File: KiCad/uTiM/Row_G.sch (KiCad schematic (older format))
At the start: 10 parts, among them U701 APA102, U702 APA102, U703 APA102, U704 APA102, U705 APA102, U706 APA102, U707 APA102, U708 APA102

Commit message: microTiM aka uTiM work in progress
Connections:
- net CO_G renamed CI_H
- net DO_G renamed DI_H
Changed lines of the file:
@@
 DI_G
 Text HLabel 950  3100 0    60   Output ~ 12
-CO_G
+CI_H
 Text HLabel 950  2350 0    60   Input ~ 12
 GND
@@
 5V
 Text Label 1075 3100 0    60   ~ 0
-CO_G
+CI_H
 $Comp
 L GND #PWR05
@@
 	10950 3350 950  3350
 Text HLabel 950  3350 0    60   Output ~ 12
-DO_G
+DI_H
 Text HLabel 950  1400 0    60   Input ~ 12
 DI_G
@@
 	1300 1600 950  1600
 Text Label 1075 3350 0    60   ~ 0
-DO_G
+DI_H
 Text Label 1075 1600 0    60   ~ 0
 CI_G

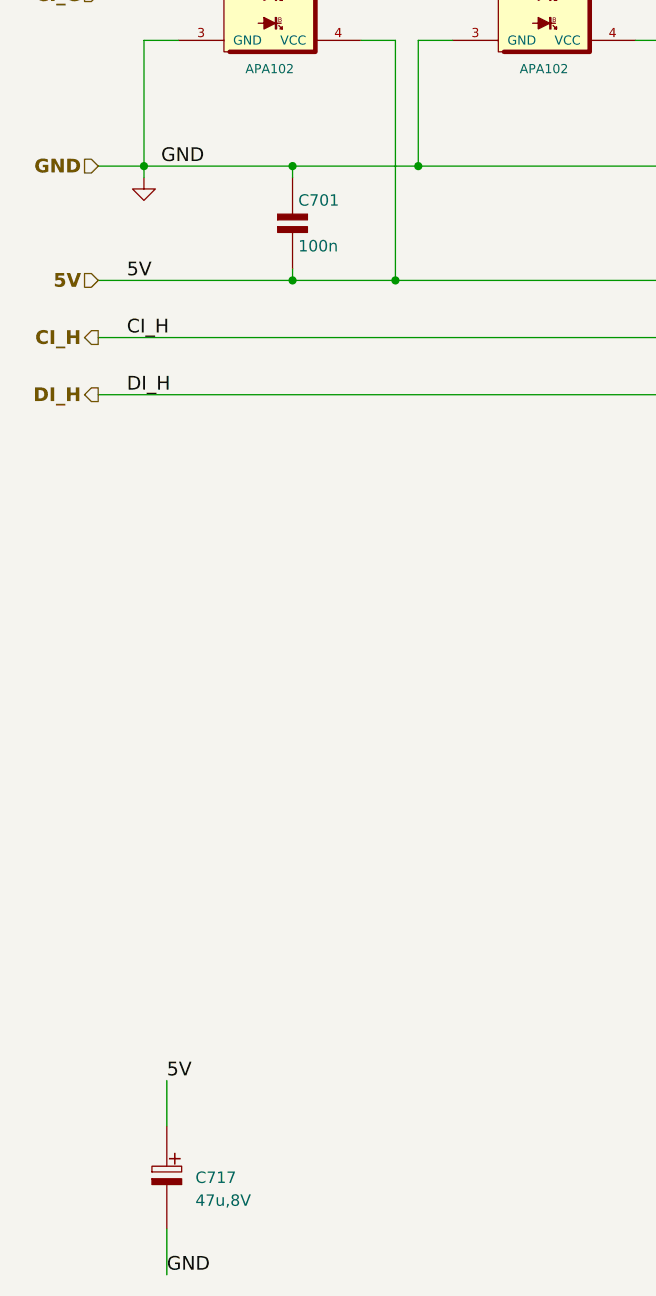
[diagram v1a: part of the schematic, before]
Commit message: work in progress, microTIM using APA102
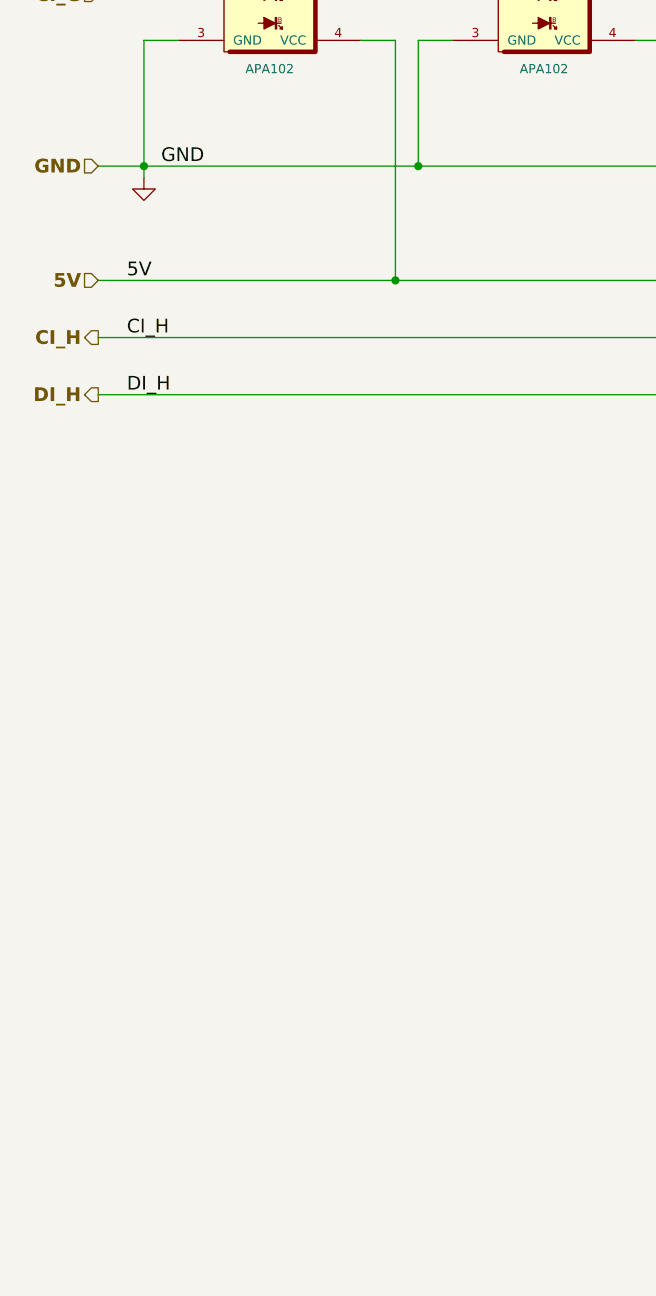
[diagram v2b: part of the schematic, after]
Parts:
- removed C701: 100n, TinyTiM_Libs:c_0805, symbol C2
- removed C717: 47u,8V, TinyTiM_Libs:c_2917, symbol C_POL_1
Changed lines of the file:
@@
 Comment4 ""
 $EndDescr
-$Comp
-L C2 C701
-U 1 1 5118AB56
-P 1800 2600
-F 0 "C701" H 1825 2700 50  0000 L CNN
-F 1 "100n" H 1825 2500 50  0000 L CNN
-F 2 "TinyTiM_Libs:c_0805" H 1800 2600 50  0001 C CNN
-F 3 "" H 1800 2600 60  0001 C CNN
-F 4 "CAP CER 0.1UF 25V 10% X7R 0805" H 1800 2800 60  0001 L CNN "Field4"
-F 5 "100nF, 25V" H 1800 2900 60  0001 L CNN "Field5"
-F 6 "Surface Mount, MLCC" H 1800 3000 60  0001 L CNN "Field6"
-F 7 "Kemet" H 1800 3100 60  0001 L CNN "Field7"
-F 8 "C0805C104K3RACTU" H 1800 3200 60  0001 L CNN "Field8"
-F 9 "Digikey" H 1800 3300 60  0001 L CNN "Field9"
-F 10 "399-1168-1-ND" H 1800 3400 60  0001 L CNN "Field10"
-F 11 "http://www.digikey.com/product-detail/en/C0805C104K3RACTU/399-1168-1-ND/411443" H 1800 3500 60  0001 L CNN "Field11"
-	1    1800 2600
-	1    0    0    -1
-$EndComp
-Text Label 1250 6350 0    60   ~ 0
-5V
-Text Label 1250 7200 0    60   ~ 0
-GND
-$Comp
-L C_POL_1 C717
-U 1 1 5118AB60
-P 1250 6750
-F 0 "C717" H 1375 6725 50  0000 L CNN
-F 1 "47u,8V" H 1375 6625 50  0000 L CNN
-F 2 "TinyTiM_Libs:c_2917" H 1250 6700 50  0001 C CNN
-F 3 "" H 1250 6750 60  0001 C CNN
-F 4 "CAP ALUM 47UF 8V 20% SMD" H 1250 6950 60  0001 L CNN "Field4"
-F 5 "47u,8V" H 1250 7050 60  0001 L CNN "Field5"
-F 6 "2917 (7343 Metric)" H 1250 7150 60  0001 L CNN "Field6"
-F 7 "Panasonic Electronic Components" H 1250 7250 60  0001 L CNN "Field7"
-F 8 "EEF-CD0K470R" H 1250 7350 60  0001 L CNN "Field8"
-F 9 "Digikey" H 1250 7450 60  0001 L CNN "Field9"
-F 10 "PCE3606CT-ND" H 1250 7550 60  0001 L CNN "Field10"
-F 11 "http://www.digikey.com/product-detail/en/EEF-CD0K470R/PCE3606CT-ND/614442" H 1250 7650 60  0001 L CNN "Field11"
-	1    1250 6750
-	1    0    0    -1
-$EndComp
-Wire Wire Line
-	1250 7000 1250 7200
-Wire Wire Line
-	1250 6550 1250 6350
 Text Label 1075 1400 0    60   ~ 0
 DI_G
@@
 Wire Wire Line
 	1150 1800 1150 2400
-Connection ~ 1800 2850
-Wire Wire Line
-	1800 2850 1800 2800
 Wire Wire Line
 	950  3100 10800 3100
-Connection ~ 1800 2350
 Wire Wire Line
 	950  2350 9550 2350
@@
 	10800 3100 10800 1600
 Wire Wire Line
-	1800 2350 1800 2400
-Wire Wire Line
 	950  2850 10650 2850

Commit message: layout complete. Gerbers pending
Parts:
- renumbered U701 to U49, U702 to U50, U703 to U51, U704 to U52, U705 to U53, U706 to U54, U707 to U55, U708 to U56
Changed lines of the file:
@@
 GND
 $Comp
-L APA102 U701
+L APA102 U49
 U 1 1 56C1D372
 P 1700 1600
-F 0 "U701" H 1700 1900 40  0000 C CNB
+F 0 "U49" H 1700 1900 40  0000 C CNB
 F 1 "APA102" H 1700 1275 40  0000 C CNN
 F 2 "TinyTiM_Libs:APA102" H 1600 2000 60  0001 C CNN
@@
 5V
 $Comp
-L APA102 U702
+L APA102 U50
 U 1 1 56C1D39D
 P 2900 1600
-F 0 "U702" H 2900 1900 40  0000 C CNB
+F 0 "U50" H 2900 1900 40  0000 C CNB
 F 1 "APA102" H 2900 1275 40  0000 C CNN
 F 2 "TinyTiM_Libs:APA102" H 2800 2000 60  0001 C CNN
@@
 $EndComp
 $Comp
-L APA102 U703
+L APA102 U51
 U 1 1 56C1D3A5
 P 4100 1600
-F 0 "U703" H 4100 1900 40  0000 C CNB
+F 0 "U51" H 4100 1900 40  0000 C CNB
 F 1 "APA102" H 4100 1275 40  0000 C CNN
 F 2 "TinyTiM_Libs:APA102" H 4000 2000 60  0001 C CNN
@@
 $EndComp
 $Comp
-L APA102 U704
+L APA102 U52
 U 1 1 56C1D3AD
 P 5300 1600
-F 0 "U704" H 5300 1900 40  0000 C CNB
+F 0 "U52" H 5300 1900 40  0000 C CNB
 F 1 "APA102" H 5300 1275 40  0000 C CNN
 F 2 "TinyTiM_Libs:APA102" H 5200 2000 60  0001 C CNN
@@
 $EndComp
 $Comp
-L APA102 U705
+L APA102 U53
 U 1 1 56C1D3B5
 P 6500 1600
-F 0 "U705" H 6500 1900 40  0000 C CNB
+F 0 "U53" H 6500 1900 40  0000 C CNB
 F 1 "APA102" H 6500 1275 40  0000 C CNN
 F 2 "TinyTiM_Libs:APA102" H 6400 2000 60  0001 C CNN
@@
 $EndComp
 $Comp
-L APA102 U706
+L APA102 U54
 U 1 1 56C1D3BD
 P 7700 1600
-F 0 "U706" H 7700 1900 40  0000 C CNB
+F 0 "U54" H 7700 1900 40  0000 C CNB
 F 1 "APA102" H 7700 1275 40  0000 C CNN
 F 2 "TinyTiM_Libs:APA102" H 7600 2000 60  0001 C CNN
@@
 $EndComp
 $Comp
-L APA102 U707
+L APA102 U55
 U 1 1 56C1D3C5
 P 8900 1600
-F 0 "U707" H 8900 1900 40  0000 C CNB
+F 0 "U55" H 8900 1900 40  0000 C CNB
 F 1 "APA102" H 8900 1275 40  0000 C CNN
 F 2 "TinyTiM_Libs:APA102" H 8800 2000 60  0001 C CNN
@@
 $EndComp
 $Comp
-L APA102 U708
+L APA102 U56
 U 1 1 56C1D3CD
 P 10100 1600
-F 0 "U708" H 10100 1900 40  0000 C CNB
+F 0 "U56" H 10100 1900 40  0000 C CNB
 F 1 "APA102" H 10100 1275 40  0000 C CNN
 F 2 "TinyTiM_Libs:APA102" H 10000 2000 60  0001 C CNN
